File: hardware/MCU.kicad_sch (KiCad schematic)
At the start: 0 parts

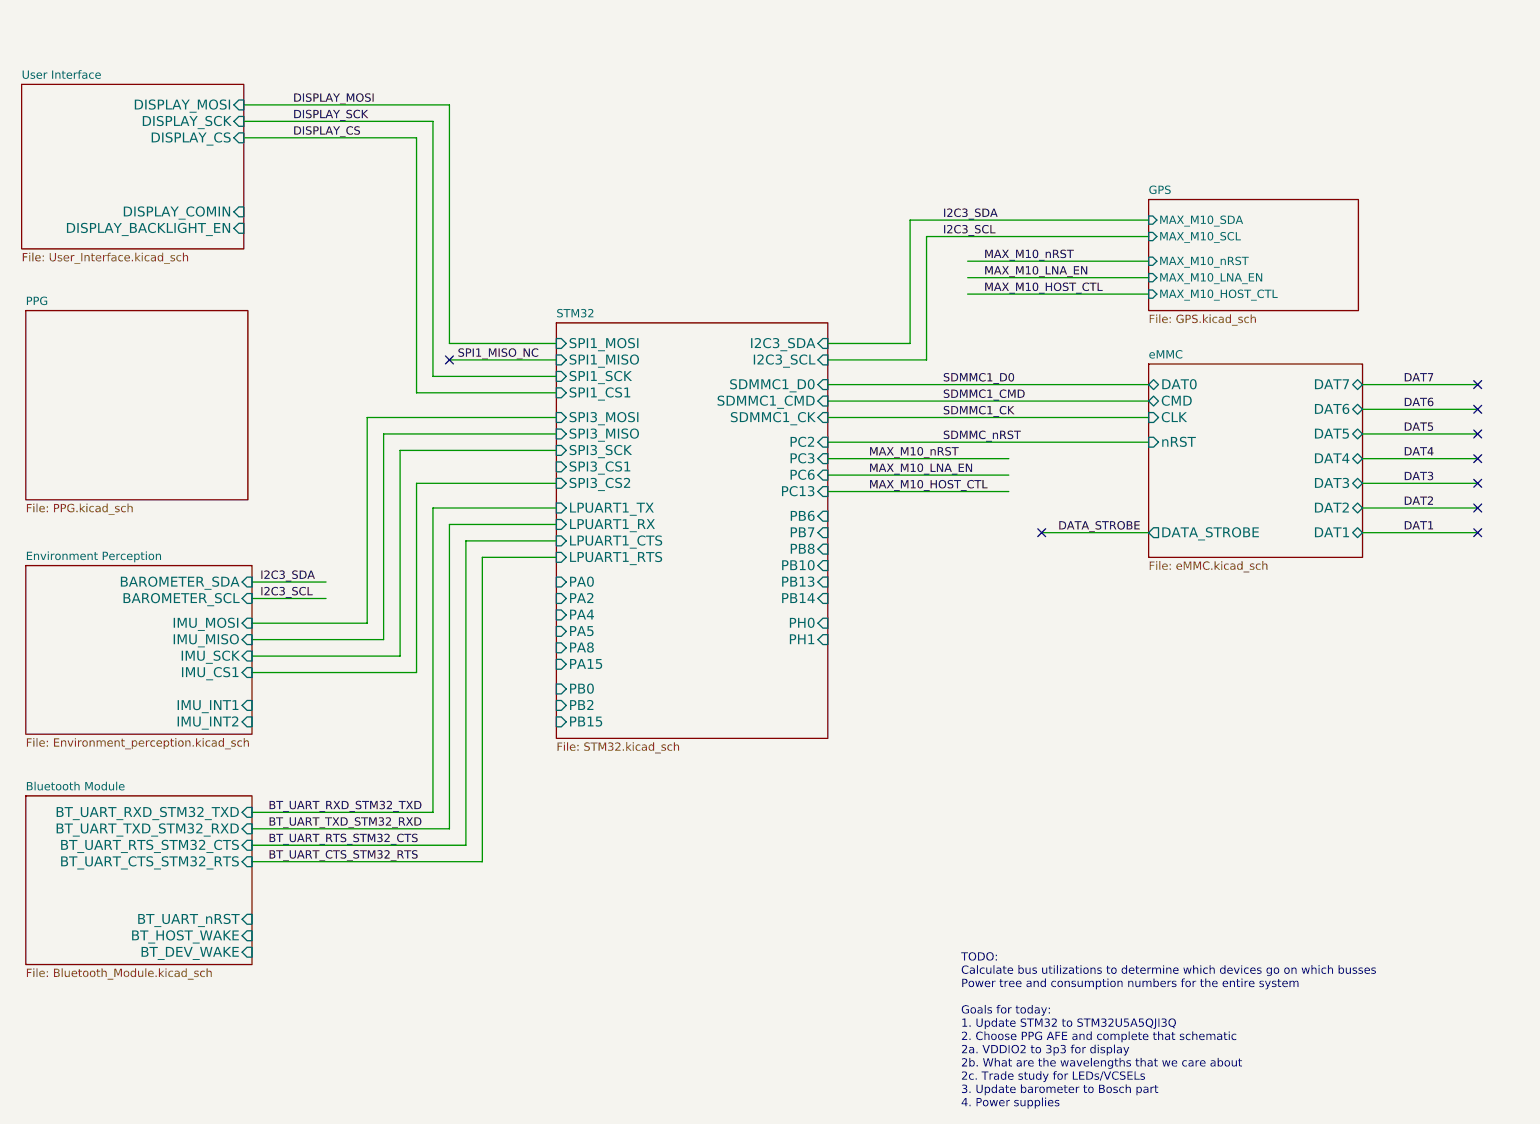
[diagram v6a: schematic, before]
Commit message: Updated schematic to add AFE4403
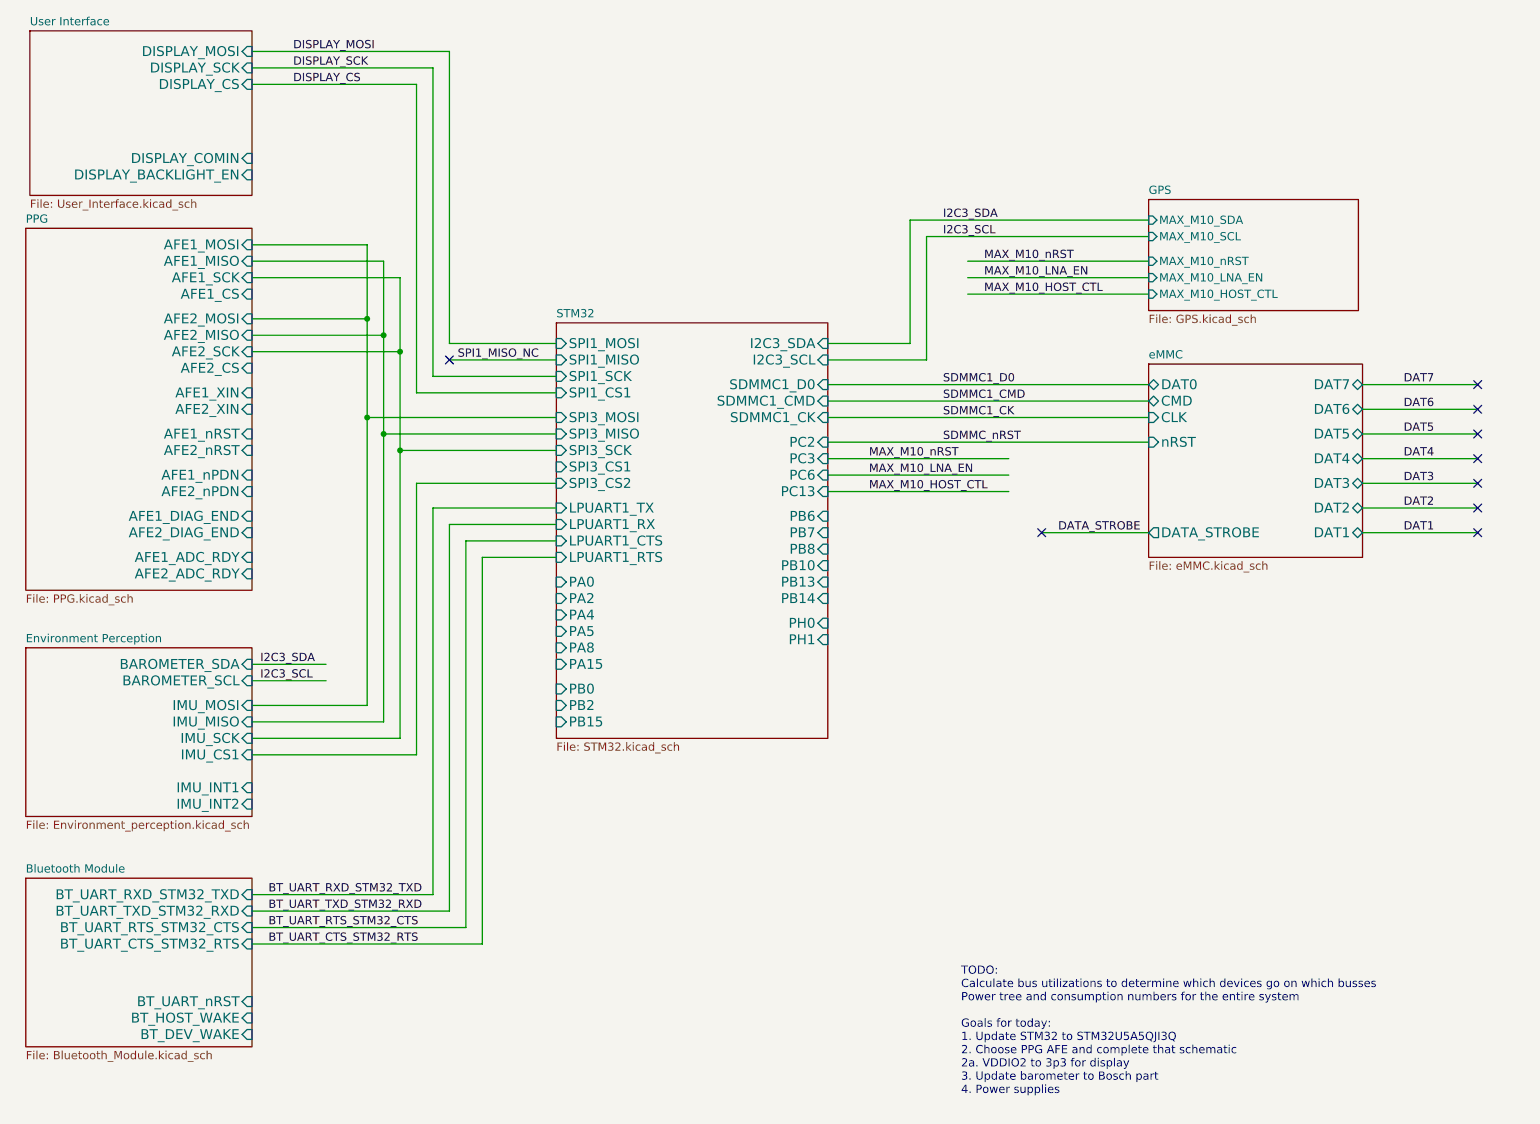
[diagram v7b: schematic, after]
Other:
- sheet PPG ports: added AFE1_ADC_RDY, AFE1_CS, AFE1_DIAG_END, AFE1_MISO, AFE1_MOSI, AFE1_SCK, AFE1_XIN, AFE1_nPDN, AFE1_nRST, AFE2_ADC_RDY, AFE2_CS, AFE2_DIAG_END, AFE2_MISO, AFE2_MOSI, AFE2_SCK, AFE2_XIN, AFE2_nPDN, AFE2_nRST; removed none
- note added: "TODO: Calculate bus utilizations to determine which devices go on which busses Power tree and consumption numbers for the entire system Goals for today: 1. Update STM32 to STM32U5A5QJI3Q 2. Choose PPG AFE and complete that schematic 2a. VDDIO2 to 3p3 for display 3. Update barometer to Bosch part 4. Power supplies"
- note removed: "TODO: Calculate bus utilizations to determine which devices go on which busses Power tree and consumption numbers for the entire system Goals for today: 1. Update STM32 to STM32U5A5QJI3Q 2. Choose PPG AFE and complete that schematic 2a. VDDIO2 to 3p3 for display 2b. What are the wavelengths that we care about 2c. Trade study for LEDs/VCSELs 3. Update barometer to Bosch part 4. Power supplies"

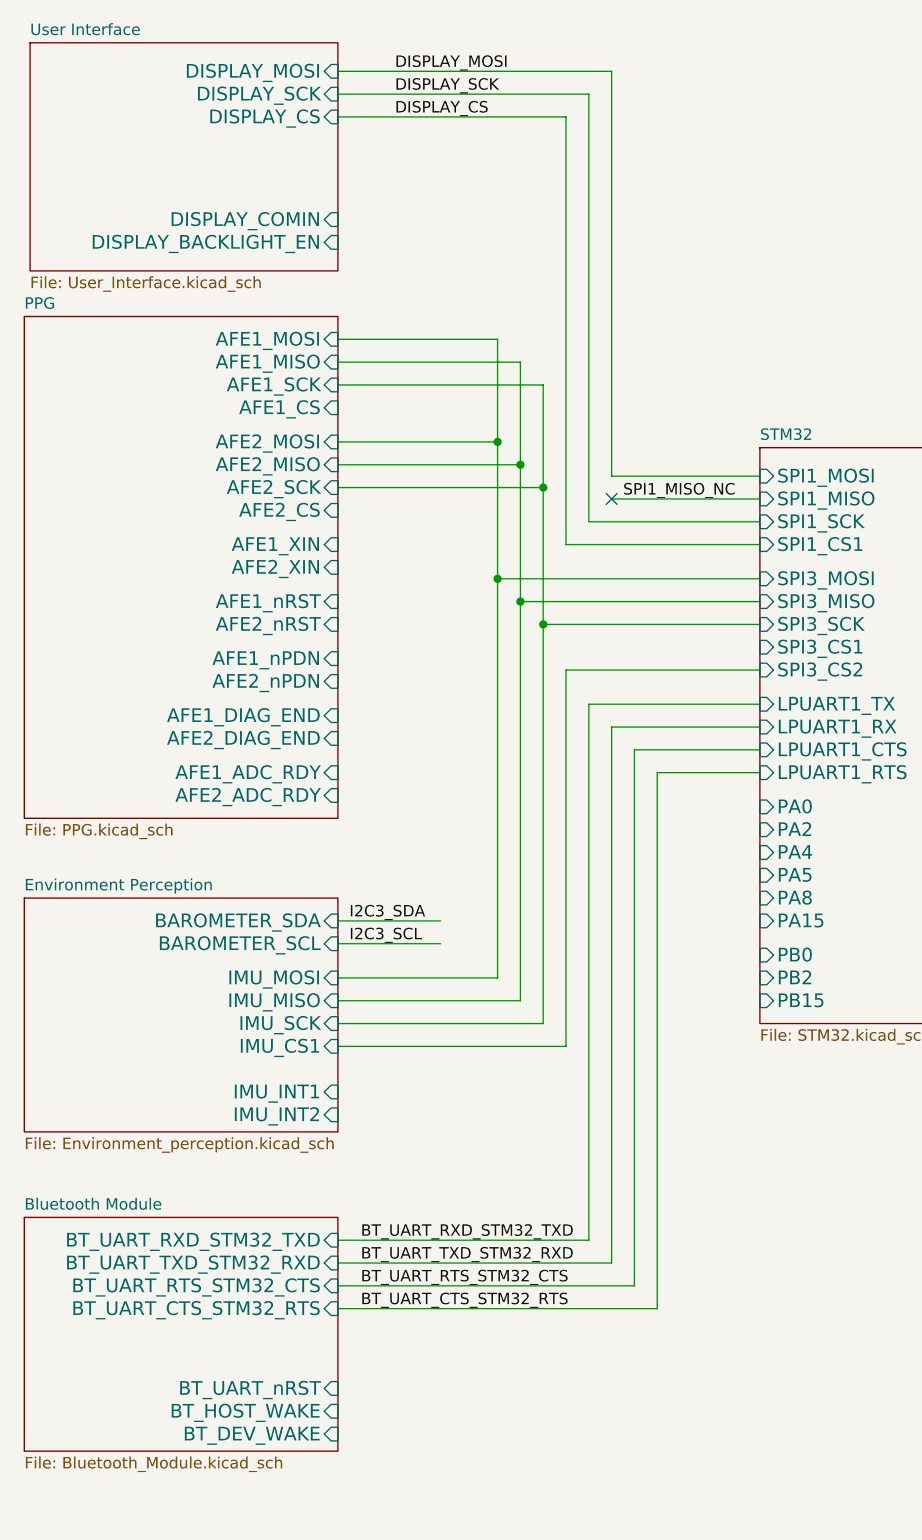
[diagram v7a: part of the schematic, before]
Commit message: Added optical front end submodule and reconnected to STM32
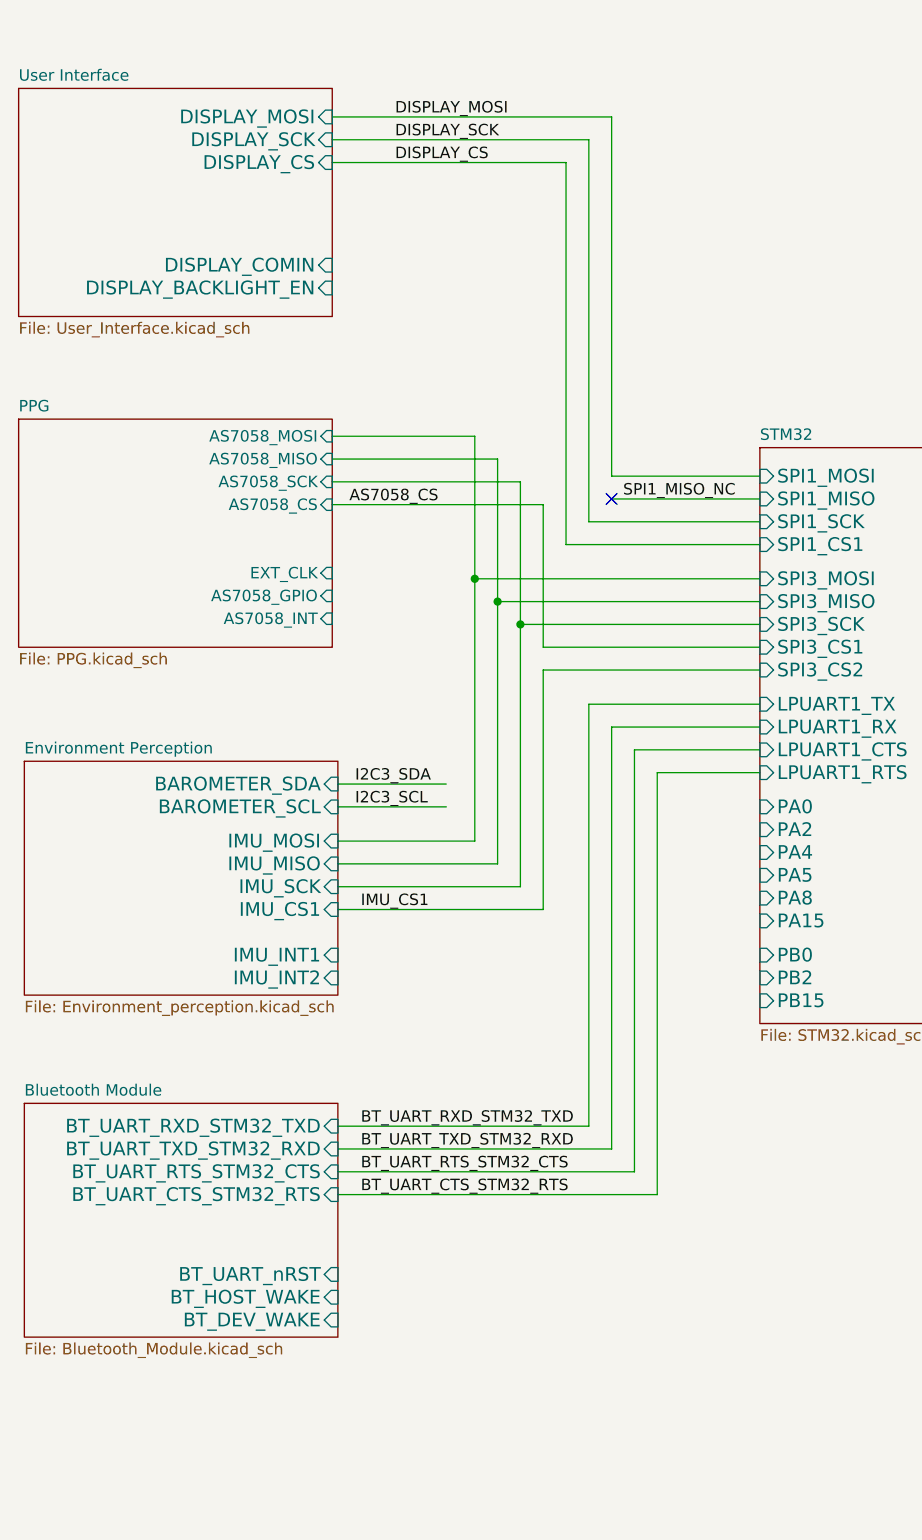
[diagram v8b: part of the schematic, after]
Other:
- sheet PPG ports: added AS7058_CS, AS7058_GPIO, AS7058_INT, AS7058_MISO, AS7058_MOSI, AS7058_SCK, EXT_CLK; removed AFE1_ADC_RDY, AFE1_CS, AFE1_DIAG_END, AFE1_MISO, AFE1_MOSI, AFE1_SCK, AFE1_XIN, AFE1_nPDN, AFE1_nRST, AFE2_ADC_RDY, AFE2_CS, AFE2_DIAG_END, AFE2_MISO, AFE2_MOSI, AFE2_SCK, AFE2_XIN, AFE2_nPDN, AFE2_nRST
